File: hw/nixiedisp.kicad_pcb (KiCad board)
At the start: 2 copper layers, 140 x 94.1 mm, 247 parts, among them J1 12VDC IN, J2 USB_B_Micro, J3 AVR-ISP-6, J4 pwr sw, J5 HRLEDS, Q1 MMBTA55, Q10 MMBTA42, Q11 MMBTA42, Q12 MMBTA42, Q13 MMBTA42, Q14 MMBTA42, Q15 MMBTA42, Q16 MMBTA42, Q17 MMBTA42, Q18 MMBTA42, Q19 MMBTA42, Q2 IRF740, Q20 MMBTA42, Q21 MMBTA42, Q22 MMBTA42, Q23 MMBTA42, Q24 MMBTA42, Q25 MMBTA42, Q26 MMBTA42, Q27 MMBTA42, Q28 MMBTA42, Q29 MMBTA42, Q3 MMBTA42, Q30 MMBTA42, Q31 MMBTA42, Q32 MMBTA42, Q33 MMBTA42, Q34 MMBTA42, Q35 MMBTA42, Q36 MMBTA42, Q37 MMBTA42, Q38 MMBTA42, Q39 MMBTA42, Q4 MMBTA42, Q40 MMBTA42, Q41 MMBTA42, Q42 MMBTA42, Q43 MMBTA42, Q44 MMBTA42, Q45 MMBTA42, Q46 MMBTA42, Q47 MMBTA42, Q48 MMBTA42, Q49 MMBTA42, Q5 MMBTA42, Q50 MMBTA42, Q51 MMBTA42, Q52 MMBTA42, Q53 MMBTA42, Q54 MMBTA42, Q55 MMBTA42, Q56 MMBTA42, Q57 MMBTA42, Q58 MMBTA42, Q59 MMBTA42, Q6 MMBTA42, Q60 MMBTA42, Q61 MMBTA42, Q62 MMBTA42, Q63 MMBTA42, Q64 MMBTA42, Q65 MMBTA42, Q66 MMBTA42, Q67 MMBTA42, Q68 MMBTA42, Q7 MMBTA42, Q8 MMBTA42, Q9 MMBTA42, U1 ATmega328P-AU, U10 IN14, U11 IN14, U12 IN14, U13 IN14, U14 74HC154, U15 74HC04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

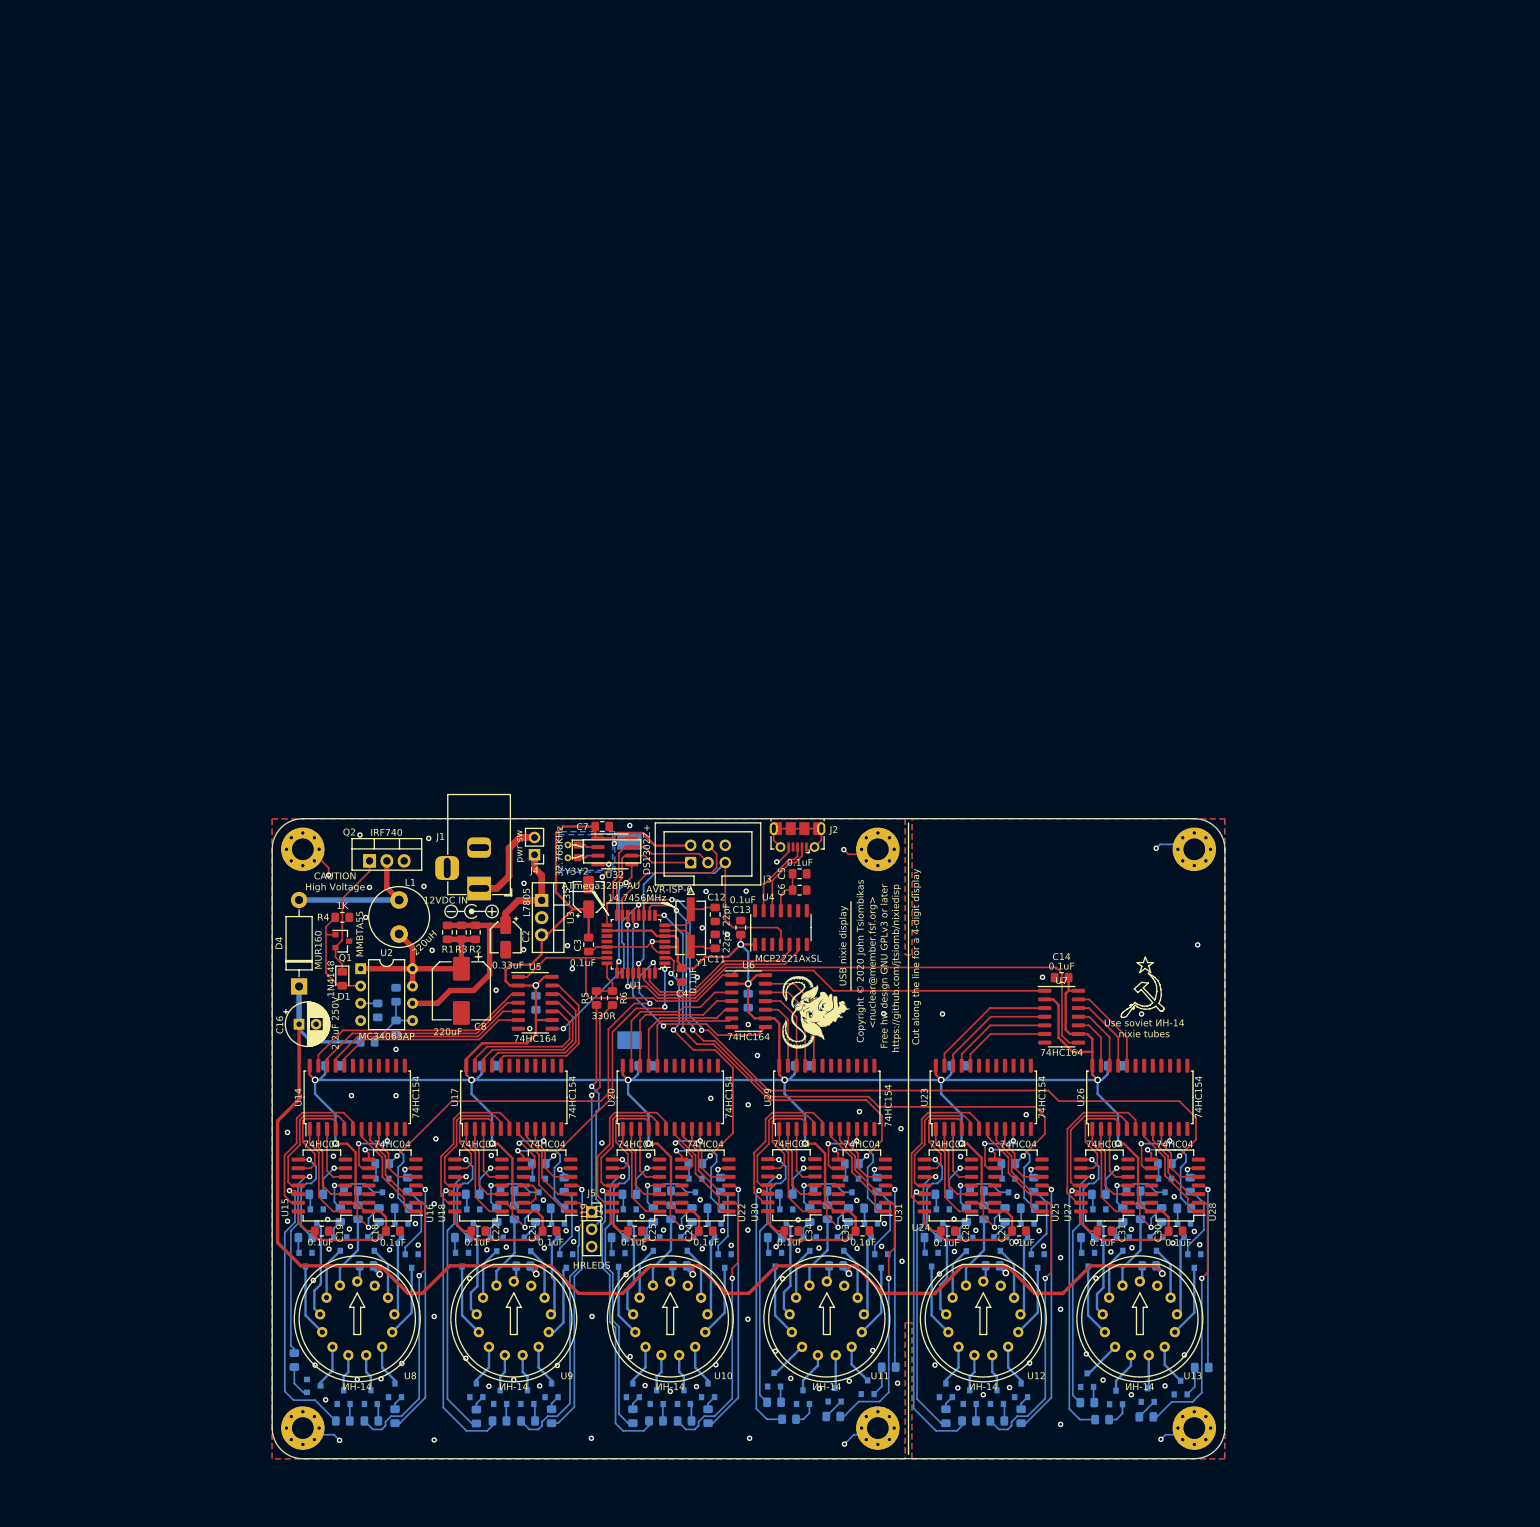
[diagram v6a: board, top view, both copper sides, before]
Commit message: lots of changes, redesigning most of the PCB
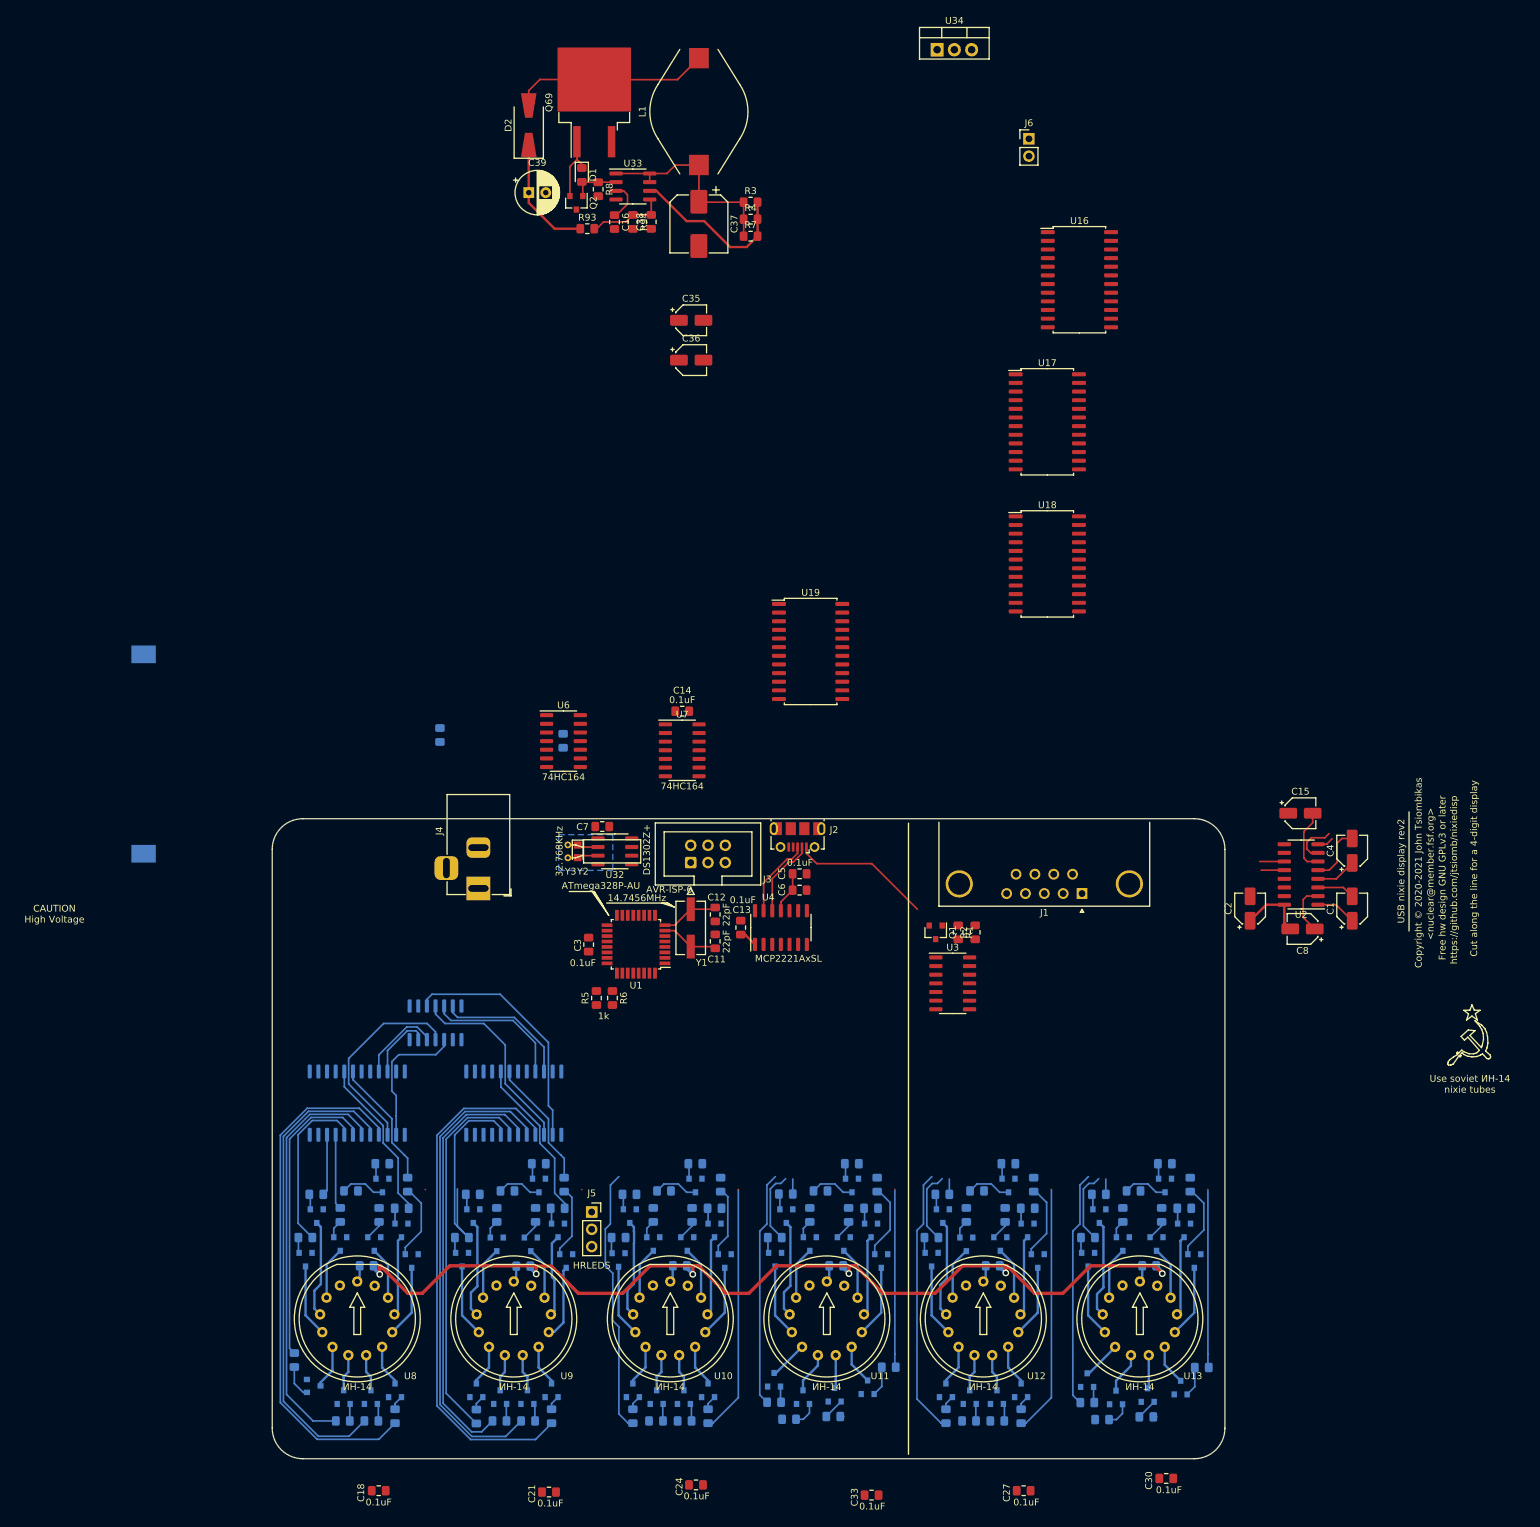
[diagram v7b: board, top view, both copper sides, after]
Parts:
- removed C17, C19, C20, C22, C23, C25, C26, C28, C29, C31, C32, C34: 0.1uF, Capacitor_SMD:C_0805_2012Metric_Pad1.15x1.40mm_HandSolder
- removed D4: MUR160, Diode_THT:D_DO-15_P12.70mm_Horizontal
- removed G***: LOGO, nixiedisp:gnulogo
- removed R27, R40, R53, R66, R79, R92: 47k, Resistor_SMD:R_0805_2012Metric_Pad1.15x1.40mm_HandSolder
- removed REF**: Symbol_Barrel_Polarity, Symbol:Symbol_Barrel_Polarity
- removed REF** (x6): M3, MountingHole:MountingHole_3.2mm_M3_Pad_Via
- removed U20, U23, U26, U29: 74HC154, Package_SO:SOIC-24W_7.5x15.4mm_P1.27mm
- removed U21, U22, U24, U25, U27, U28, U30, U31: 74HC04, Package_SO:SO-14_5.3x10.2mm_P1.27mm
- added C36: 0.33uF, Capacitor_SMD:CP_Elec_4x5.4, F.Cu at (130.1, -15.9)
- added C37: 220uF, Capacitor_SMD:CP_Elec_8x10, F.Cu at (131.2, -35.9)
- added C38: 10nF, Capacitor_SMD:C_0805_2012Metric_Pad1.15x1.40mm_HandSolder, F.Cu at (124.2, -36.2)
- added C39: 2.2uF 250V, Capacitor_THT:CP_Radial_D6.3mm_P2.50mm, F.Cu at (106.2, -40.5)
- added D2: MUR160, Diode_SMD:D_SMA-SMB_Universal_Handsoldering, F.Cu at (106.2, -50.4)
- added J6: pwr sw, Connector_PinHeader_2.54mm:PinHeader_1x02_P2.54mm_Vertical, F.Cu at (179.7, -48.4)
- added Q69: IRF740, Package_TO_SOT_SMD:TO-263-2, F.Cu at (115.8, -53.8)
- added R93: 475K, Resistor_SMD:R_0805_2012Metric_Pad1.15x1.40mm_HandSolder, F.Cu at (114.8, -35.2)
- added R94: 3K32, Resistor_SMD:R_0805_2012Metric_Pad1.15x1.40mm_HandSolder, F.Cu at (121.5, -36.2)
- added U33: MC34063AD, Package_SO:SOIC-8_3.9x4.9mm_P1.27mm, F.Cu at (121.5, -41.4)
- added U34: L7805, Package_TO_SOT_THT:TO-220-3_Vertical, F.Cu at (166.2, -61.5)
- C1: value 2.2nF -> 1uF; footprint Capacitor_SMD:C_0805_2012Metric_Pad1.15x1.40mm_HandSolder -> Capacitor_SMD:CP_Elec_4x3.9; moved to F.Cu
- C15: value 10nF -> 1uF; footprint Capacitor_SMD:C_0805_2012Metric_Pad1.15x1.40mm_HandSolder -> Capacitor_SMD:CP_Elec_4x3.9; moved to F.Cu
- C16: value 2.2uF 250V -> 2.2nF; footprint Capacitor_THT:CP_Radial_D6.3mm_P2.50mm -> Capacitor_SMD:C_0805_2012Metric_Pad1.15x1.40mm_HandSolder
- C2: value 0.33uF -> 1uF; footprint Capacitor_SMD:CP_Elec_4x5.4 -> Capacitor_SMD:CP_Elec_4x3.9
- C4: value 0.1uF -> 1uF; footprint Capacitor_SMD:C_0805_2012Metric_Pad1.15x1.40mm_HandSolder -> Capacitor_SMD:CP_Elec_4x3.9
- C8: value 220uF -> 1uF; footprint Capacitor_SMD:CP_Elec_8x10 -> Capacitor_SMD:CP_Elec_4x3.9
- J1: value 12VDC IN -> serial port; footprint Connector_BarrelJack:BarrelJack_Horizontal -> Connector_Dsub:DSUB-9_Male_Horizontal_P2.77x2.84mm_EdgePinOffset7.70mm_Housed_MountingHolesOffset9.12mm
- J4: value pwr sw -> 12VDC IN; footprint Connector_PinHeader_2.54mm:PinHeader_1x02_P2.54mm_Vertical -> Connector_BarrelJack:BarrelJack_Horizontal
- L1: footprint Inductor_THT:L_Radial_D8.7mm_P5.00mm_Fastron_07HCP -> Inductor_SMD:L_Bourns_SDR1806
- Q2: value IRF740 -> MMBTA55; footprint Package_TO_SOT_THT:TO-220-3_Vertical -> Package_TO_SOT_SMD:SOT-23
- R1, R2: value 1R -> 10k
- R10, R11, R12, R13, R14, R9: value 30k -> 24k
- R21, R34, R47, R60, R73, R86: value 47k -> 160k
- R4: value 1K -> 1R
- R5, R6: value 330R -> 1k
- R7: value 475K -> 1R; moved to F.Cu
- R8: value 3K32 -> 1K; moved to F.Cu
- U14: value 74HC154 -> 74HC4514; moved to B.Cu
- U15: value 74HC04 -> 74HC4514; footprint Package_SO:SO-14_5.3x10.2mm_P1.27mm -> Package_SO:SOIC-24W_7.5x15.4mm_P1.27mm; moved to B.Cu
- U16, U18, U19: value 74HC04 -> 74HC4514; footprint Package_SO:SO-14_5.3x10.2mm_P1.27mm -> Package_SO:SOIC-24W_7.5x15.4mm_P1.27mm
- U17: value 74HC154 -> 74HC4514
- U2: value MC34063AP -> MAX232; footprint Package_DIP:DIP-8_W7.62mm -> Package_SO:SOIC-16_3.9x9.9mm_P1.27mm
- U3: value L7805 -> 74HC126; footprint Package_TO_SOT_THT:TO-220-3_Vertical -> Package_SO:SOIC-14_3.9x8.7mm_P1.27mm
- U5: moved to B.Cu
- moved U16 167.1 mm to (187.1, -27.7), turned to 0 degrees
- moved C1 144.0 mm to (227.2, 64.7), turned to 90 degrees
- moved U2 138.9 mm to (219.7, 59.7), turned to 180 degrees
- moved C15 136.6 mm to (219.6, 50.7), turned to 0 degrees
- moved R7 131.1 mm to (138.8, -34.1)
- moved L1 128.6 mm to (131.2, -52.4)
- moved C16 126.7 mm to (118.8, -36.2), turned to 270 degrees
- moved U17 126.5 mm to (182.4, -6.82), turned to 0 degrees
- moved C8 123.9 mm to (219.9, 67.7), turned to 180 degrees
- moved U18 123.8 mm to (182.4, 14.1), turned to 0 degrees
- moved D1 123.3 mm to (114.0, -43.1)
- moved R8 122.0 mm to (116.4, -41.0), turned to 270 degrees
- moved R4 118.9 mm to (138.8, -36.6)
- moved R3 115.4 mm to (138.8, -39.1), turned to 0 degrees
- moved C2 109.5 mm to (212.2, 64.7), turned to 90 degrees
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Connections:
- C1 pad 2: GND -> Net-(C1-Pad2)
- C16 pad 1: HT -> Net-(C16-Pad1)
- C2 pad 1: +12V -> VCC
- C35 pad 1: VCC -> +12V
- C4 pad 1: VCC -> Net-(C4-Pad1)
- C4 pad 2: GND -> Net-(C4-Pad2)
- C8 pad 2: GND -> VCC
- J1 pad 1: Net-(J1-Pad1) -> (no net)
- J1 pad 2: GND -> /RX232
- J1 pad 3: GND -> /TX232
- J2 pad 1: Net-(J2-Pad1) -> /ENUSB
- J2 pad 4: Net-(J2-Pad4) -> (no net)
- J4 pad 1: +12V -> Net-(J4-Pad1)
- J4 pad 2: Net-(J1-Pad1) -> GND
- L1 pad 1: Net-(C8-Pad1) -> Net-(C37-Pad1)
- L1 pad 2: Net-(D4-Pad2) -> Net-(D2-Pad2)
- Q1 pad 1: Net-(D1-Pad2) -> Net-(Q1-Pad1)
- Q1 pad 2: Net-(D1-Pad1) -> VCC
- Q1 pad 3: GND -> /~ENUSB
- Q2 pad 1: Net-(D1-Pad1) -> Net-(D1-Pad2)
- Q2 pad 2: Net-(D4-Pad2) -> Net-(D1-Pad1)
- R1 pad 1: Net-(C8-Pad1) -> Net-(Q1-Pad1)
- R1 pad 2: +12V -> /ENUSB
- R2 pad 1: Net-(C8-Pad1) -> /~ENUSB
- R2 pad 2: +12V -> GND
- R21 pad 1: Net-(R21-Pad1) -> /nixiedrivers/NL
- R3 pad 1: Net-(C8-Pad1) -> Net-(C37-Pad1)
- R34 pad 1: Net-(R34-Pad1) -> /nixiedrivers2/NL
- R4 pad 1: Net-(D1-Pad2) -> Net-(C37-Pad1)
- R4 pad 2: GND -> +12V
- R47 pad 1: Net-(R47-Pad1) -> /nixiedrivers3/NL
- R60 pad 1: Net-(R60-Pad1) -> /nixiedrivers5/NL
- R7 pad 1: HT -> Net-(C37-Pad1)
- R7 pad 2: Net-(C15-Pad2) -> +12V
- R73 pad 1: Net-(R73-Pad1) -> /nixiedrivers6/NL
- R8 pad 1: Net-(C15-Pad2) -> Net-(D1-Pad2)
- R86 pad 1: Net-(R86-Pad1) -> /nixiedrivers4/NL
- U1 pad 19: Net-(U1-Pad19) -> (no net)
- U1 pad 20: Net-(U1-Pad20) -> (no net)
- U1 pad 22: Net-(U1-Pad22) -> (no net)
- U1 pad 26: Net-(U1-Pad26) -> (no net)
- U1 pad 27: Net-(U1-Pad27) -> (no net)
- U1 pad 28: Net-(U1-Pad28) -> (no net)
- U10 pad 13: Net-(U10-Pad13) -> (no net)
- U11 pad 13: Net-(U11-Pad13) -> (no net)
- U12 pad 13: Net-(U12-Pad13) -> (no net)
- U13 pad 13: Net-(U13-Pad13) -> (no net)
- U14 pad 1: Net-(U14-Pad1) -> VCC
- U14 pad 10: Net-(U14-Pad10) -> Net-(R16-Pad2)
- U14 pad 11: Net-(U14-Pad11) -> Net-(R15-Pad2)
- U14 pad 13: Net-(U14-Pad13) -> (no net)
- U14 pad 14: Net-(U14-Pad14) -> (no net)
- U14 pad 15: Net-(U14-Pad15) -> (no net)
- U14 pad 16: Net-(U14-Pad16) -> (no net)
- U14 pad 17: Net-(U14-Pad17) -> Net-(R26-Pad2)
- U14 pad 18: GND -> Net-(R19-Pad2)
- U14 pad 19: GND -> (no net)
- U14 pad 2: Net-(U14-Pad2) -> /A0
- U14 pad 20: /A3 -> (no net)
- U14 pad 22: /A1 -> /A3
- U14 pad 23: /A0 -> GND
- U14 pad 3: Net-(U14-Pad3) -> /A1
- U14 pad 4: Net-(U14-Pad4) -> Net-(R25-Pad2)
- U14 pad 5: Net-(U14-Pad5) -> Net-(R18-Pad2)
- U14 pad 6: Net-(U14-Pad6) -> Net-(R24-Pad2)
- U14 pad 7: Net-(U14-Pad7) -> Net-(R17-Pad2)
- U14 pad 8: Net-(U14-Pad8) -> Net-(R23-Pad2)
- U14 pad 9: Net-(U14-Pad9) -> Net-(R22-Pad2)
- U15 pad 1: Net-(U14-Pad1) -> VCC
- U15 pad 10: Net-(R17-Pad2) -> Net-(R29-Pad2)
- U15 pad 11: Net-(U14-Pad5) -> Net-(R28-Pad2)
- U15 pad 12: Net-(R24-Pad2) -> GND
- U15 pad 13: Net-(U14-Pad6) -> (no net)
- U15 pad 14: VCC -> (no net)
- U15 pad 2: Net-(R15-Pad2) -> /B0
- U15 pad 3: Net-(U14-Pad2) -> /B1
- U15 pad 4: Net-(R22-Pad2) -> Net-(R38-Pad2)
- U15 pad 5: Net-(U14-Pad3) -> Net-(R31-Pad2)
- U15 pad 6: Net-(R16-Pad2) -> Net-(R37-Pad2)
- U15 pad 7: GND -> Net-(R30-Pad2)
- U15 pad 8: Net-(R23-Pad2) -> Net-(R36-Pad2)
- U15 pad 9: Net-(U14-Pad4) -> Net-(R35-Pad2)
- U16 pad 1: Net-(U14-Pad7) -> VCC
- U16 pad 10: Net-(U16-Pad10) -> Net-(R42-Pad2)
- U16 pad 11: GND -> Net-(R41-Pad2)
- U16 pad 12: Net-(U16-Pad12) -> GND
- U16 pad 13: GND -> (no net)
- U16 pad 14: VCC -> (no net)
- U16 pad 2: Net-(R18-Pad2) -> /C0
- U16 pad 3: Net-(U14-Pad8) -> /C1
- U16 pad 4: Net-(R25-Pad2) -> Net-(R51-Pad2)
- U16 pad 5: Net-(U14-Pad9) -> Net-(R44-Pad2)
- U16 pad 6: Net-(R19-Pad2) -> Net-(R50-Pad2)
- U16 pad 7: GND -> Net-(R43-Pad2)
- U16 pad 8: Net-(R26-Pad2) -> Net-(R49-Pad2)
- U16 pad 9: Net-(U14-Pad10) -> Net-(R48-Pad2)
- U17 pad 1: Net-(U17-Pad1) -> VCC
- U17 pad 10: Net-(U17-Pad10) -> Net-(R55-Pad2)
- U17 pad 11: Net-(U17-Pad11) -> Net-(R54-Pad2)
- U17 pad 13: Net-(U17-Pad13) -> (no net)
- U17 pad 14: Net-(U17-Pad14) -> (no net)
- U17 pad 15: Net-(U17-Pad15) -> (no net)
- U17 pad 16: Net-(U17-Pad16) -> (no net)
- U17 pad 17: Net-(U17-Pad17) -> Net-(R65-Pad2)
- U17 pad 18: GND -> Net-(R58-Pad2)
- U17 pad 19: GND -> (no net)
- U17 pad 2: Net-(U17-Pad2) -> /E0
- U17 pad 20: /B3 -> (no net)
- U17 pad 21: /B2 -> /E2
- U17 pad 22: /B1 -> /E3
- U17 pad 23: /B0 -> GND
- U17 pad 3: Net-(U17-Pad3) -> /E1
- U17 pad 4: Net-(U17-Pad4) -> Net-(R64-Pad2)
- U17 pad 5: Net-(U17-Pad5) -> Net-(R57-Pad2)
- U17 pad 6: Net-(U17-Pad6) -> Net-(R63-Pad2)
- U17 pad 7: Net-(U17-Pad7) -> Net-(R56-Pad2)
- U17 pad 8: Net-(U17-Pad8) -> Net-(R62-Pad2)
- U17 pad 9: Net-(U17-Pad9) -> Net-(R61-Pad2)
- U18 pad 1: Net-(U17-Pad1) -> VCC
- U18 pad 10: Net-(R30-Pad2) -> Net-(R68-Pad2)
- U18 pad 11: Net-(U17-Pad5) -> Net-(R67-Pad2)
- U18 pad 12: Net-(R37-Pad2) -> GND
- U18 pad 13: Net-(U17-Pad6) -> (no net)
- U18 pad 14: VCC -> (no net)
- U18 pad 2: Net-(R28-Pad2) -> /F0
- U18 pad 3: Net-(U17-Pad2) -> /F1
- U18 pad 4: Net-(R35-Pad2) -> Net-(R77-Pad2)
- U18 pad 5: Net-(U17-Pad3) -> Net-(R70-Pad2)
- U18 pad 6: Net-(R29-Pad2) -> Net-(R76-Pad2)
- U18 pad 7: GND -> Net-(R69-Pad2)
- U18 pad 8: Net-(R36-Pad2) -> Net-(R75-Pad2)
- U18 pad 9: Net-(U17-Pad4) -> Net-(R74-Pad2)
- U19 pad 1: Net-(U17-Pad7) -> VCC
- U19 pad 10: Net-(U19-Pad10) -> Net-(R81-Pad2)
- U19 pad 11: GND -> Net-(R80-Pad2)
- U19 pad 12: Net-(U19-Pad12) -> GND
- U19 pad 13: GND -> (no net)
- U19 pad 14: VCC -> (no net)
- U19 pad 2: Net-(R31-Pad2) -> /D0
- U19 pad 3: Net-(U17-Pad8) -> /D1
- U19 pad 4: Net-(R38-Pad2) -> Net-(R90-Pad2)
- U19 pad 5: Net-(U17-Pad9) -> Net-(R83-Pad2)
- U19 pad 6: Net-(R32-Pad2) -> Net-(R89-Pad2)
- U19 pad 7: GND -> Net-(R82-Pad2)
- U19 pad 8: Net-(R39-Pad2) -> Net-(R88-Pad2)
- U19 pad 9: Net-(U17-Pad10) -> Net-(R87-Pad2)
- U2 pad 1: Net-(C8-Pad1) -> Net-(C1-Pad1)
- U2 pad 2: Net-(D1-Pad2) -> Net-(C8-Pad1)
- U2 pad 3: Net-(C1-Pad1) -> Net-(C1-Pad2)
- U2 pad 4: GND -> Net-(C4-Pad1)
- U2 pad 5: Net-(C15-Pad2) -> Net-(C4-Pad2)
- U2 pad 6: +12V -> Net-(C15-Pad2)
- U2 pad 7: Net-(C8-Pad1) -> /RTS232
- U2 pad 8: Net-(C8-Pad1) -> /CTS232
- U3 pad 1: +12V -> /~ENUSB
- U3 pad 2: GND -> /SRX
- U3 pad 3: VCC -> /RXD
- U4 pad 10: Net-(U4-Pad10) -> (no net)
- U4 pad 2: Net-(U4-Pad2) -> (no net)
- U4 pad 3: Net-(U4-Pad3) -> (no net)
- U4 pad 6: /RXD -> /URX
- U4 pad 7: Net-(U4-Pad7) -> (no net)
- U4 pad 8: Net-(U4-Pad8) -> (no net)
- U4 pad 9: Net-(U4-Pad9) -> (no net)
- U8 pad 13: Net-(U8-Pad13) -> (no net)
- U9 pad 13: Net-(U9-Pad13) -> (no net)
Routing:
- net VCC: track 598.8 -> 12.6 mm, vias 15 -> 0
- net /FDOT: track 113.7 -> 0.00 mm, vias 3 -> 0
- net /SD: track 90.5 -> 0.00 mm
- net /EDOT: track 89.8 -> 0.00 mm, vias 3 -> 0
- net /CK3: track 89.2 -> 0.00 mm, vias 2 -> 0
- net /ADOT: track 62.7 -> 0.00 mm, vias 3 -> 0
- net GND: track 62.6 -> 0.14 mm, vias 148 -> 0
- net /DDOT: track 62.3 -> 0.00 mm, vias 3 -> 0
- net HT: track 213.4 -> 165.0 mm
- net /~RST: track 45.9 -> 0.00 mm, vias 1 -> 0
- net Net-(R50-Pad2): track 43.4 -> 0.00 mm, vias 1 -> 0
- net Net-(R63-Pad2): track 42.7 -> 0.00 mm, vias 1 -> 0
- net Net-(R57-Pad2): track 41.0 -> 0.00 mm, vias 1 -> 0
- net Net-(R44-Pad2): track 41.0 -> 0.00 mm, vias 1 -> 0
- net /CDOT: track 39.7 -> 0.00 mm, vias 3 -> 0
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- removed copper zone on F.Cu, net GND
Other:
- board text added: "Allakse to vreg se ksaploto, i akoma kalytera SMD"
- board text added: "Allakse ton pyknoti se ksaploto (kai cutout sto PCB?)"
- board text added: "Copyright © 2020-2021 John Tsiombikas"
- board text added: "USB nixie display rev2"
- board text removed: "Copyright © 2020 John Tsiombikas"
- board text removed: "USB nixie display"

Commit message: PCB rev2 layout in progress
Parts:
- added SW1: SW_MODE, nixiedisp:switch, F.Cu at (118.5, 142.8)
- added SW2: SW_A, nixiedisp:switch, F.Cu at (138.5, 142.8)
- added SW3: SW_B, nixiedisp:switch, F.Cu at (158.5, 142.8)
- C39: footprint Capacitor_THT:CP_Radial_D6.3mm_P2.50mm -> nixiedisp:CP_Radial_D6.3mm_P2.50mm_Horizontal
- U16, U17, U18, U19: moved to B.Cu
- U34: footprint Package_TO_SOT_THT:TO-220-3_Vertical -> Package_TO_SOT_SMD:TO-252-2
- U5: moved to F.Cu
- moved R3 203.7 mm to (39.6, 138.8), turned to 270 degrees
- moved R4 202.8 mm to (37.1, 138.8), turned to 270 degrees
- moved R7 201.9 mm to (34.6, 138.8), turned to 270 degrees
- moved L1 199.6 mm to (52.9, 131.2), turned to 0 degrees
- moved C37 192.1 mm to (36.4, 131.2), turned to 180 degrees
- moved C38 182.7 mm to (36.7, 124.2), turned to 0 degrees
- moved U33 181.3 mm to (41.9, 121.5), turned to 270 degrees
- moved Q69 180.4 mm to (54.2, 115.8), turned to 0 degrees
- moved R94 179.1 mm to (36.7, 121.5), turned to 180 degrees
- moved C16 175.4 mm to (36.7, 118.8), turned to 180 degrees
- moved R8 174.3 mm to (41.5, 116.4), turned to 180 degrees
- moved D1 172.2 mm to (43.6, 114.0), turned to 180 degrees
- moved R93 169.6 mm to (35.7, 114.8), turned to 270 degrees
- moved Q2 169.1 mm to (39.5, 113.2), turned to 180 degrees
- moved D2 166.1 mm to (50.9, 106.2), turned to 0 degrees
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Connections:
- net Net-(D2-Pad2) renamed /pwrsupply/TPAD
- U1 pad 26: (no net) -> /SWMODE
- U1 pad 27: (no net) -> /SWA
- U1 pad 28: (no net) -> /SWB
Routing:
- net /SD: track 0.00 -> 135.3 mm
- net /FDOT: track 0.00 -> 97.9 mm, vias 0 -> 3
- net /CK3: track 0.00 -> 95.2 mm
- net /SWB: track 0.00 -> 86.2 mm, vias 0 -> 2
- net /EDOT: track 0.00 -> 74.9 mm, vias 0 -> 3
- net Net-(R83-Pad2): track 0.53 -> 73.1 mm
- net Net-(R70-Pad2): track 0.53 -> 71.0 mm
- net Net-(R57-Pad2): track 0.00 -> 69.4 mm
- net Net-(R44-Pad2): track 0.00 -> 68.6 mm
- net /SWA: track 0.00 -> 67.7 mm, vias 0 -> 2
- net Net-(R90-Pad2): track 26.2 -> 89.5 mm
- net Net-(R63-Pad2): track 0.00 -> 61.8 mm
- net Net-(R77-Pad2): track 26.2 -> 87.2 mm
- net Net-(R50-Pad2): track 0.00 -> 60.8 mm
- net Net-(R89-Pad2): track 0.00 -> 59.3 mm
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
